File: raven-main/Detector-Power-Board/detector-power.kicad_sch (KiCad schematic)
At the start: 37 parts, among them J1 DeployLipo, J2 Conn_01x04, J9 UCLipo, U1 LT8330IS6-TRMPBF, U2 TPS22810DRV, U3 LM317LCLPRE3, U4 LM317LCLPRE3

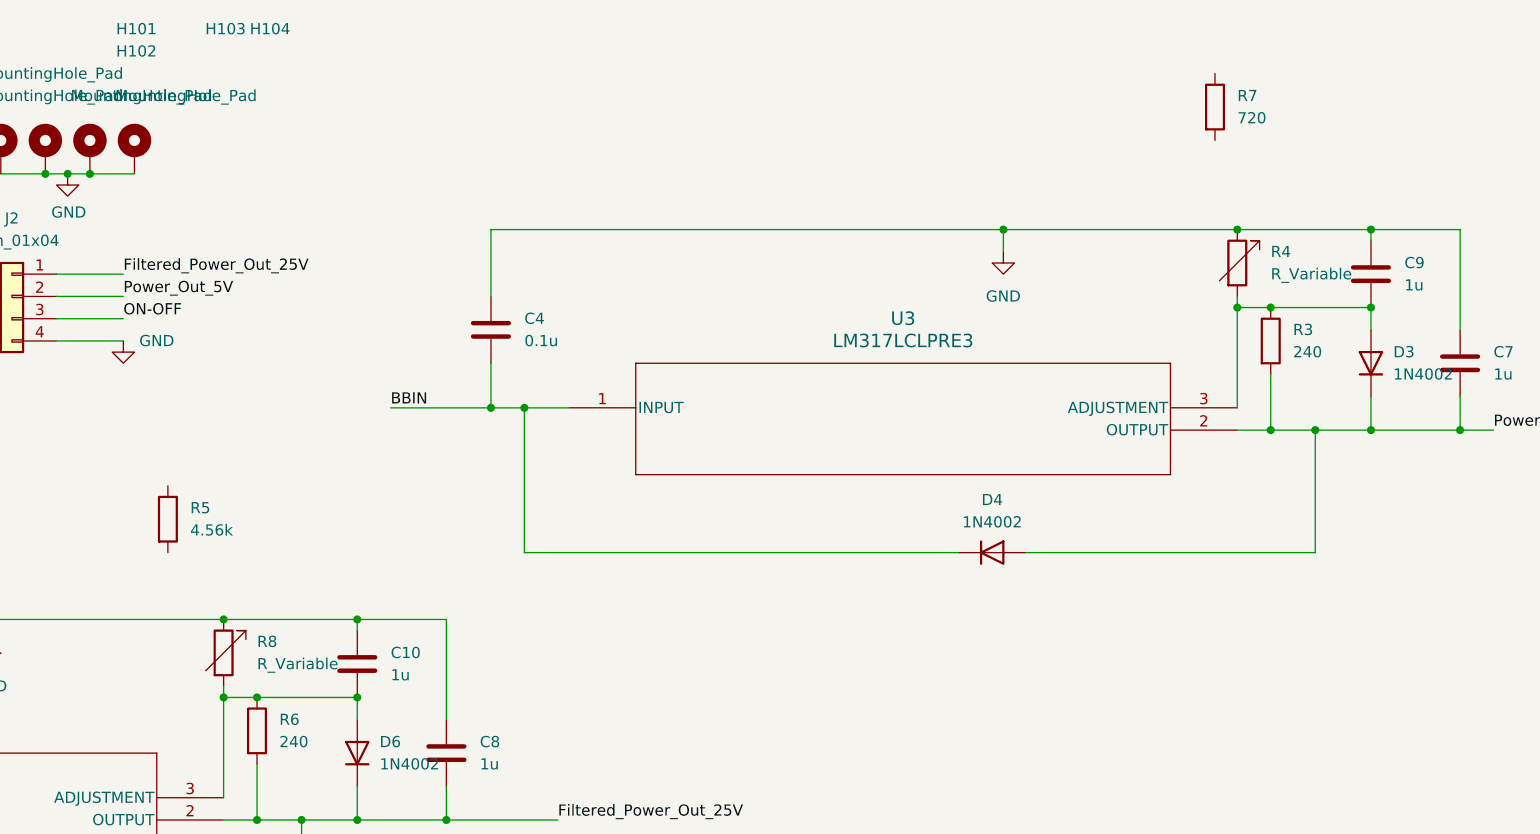
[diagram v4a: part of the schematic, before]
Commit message: More efficient routing
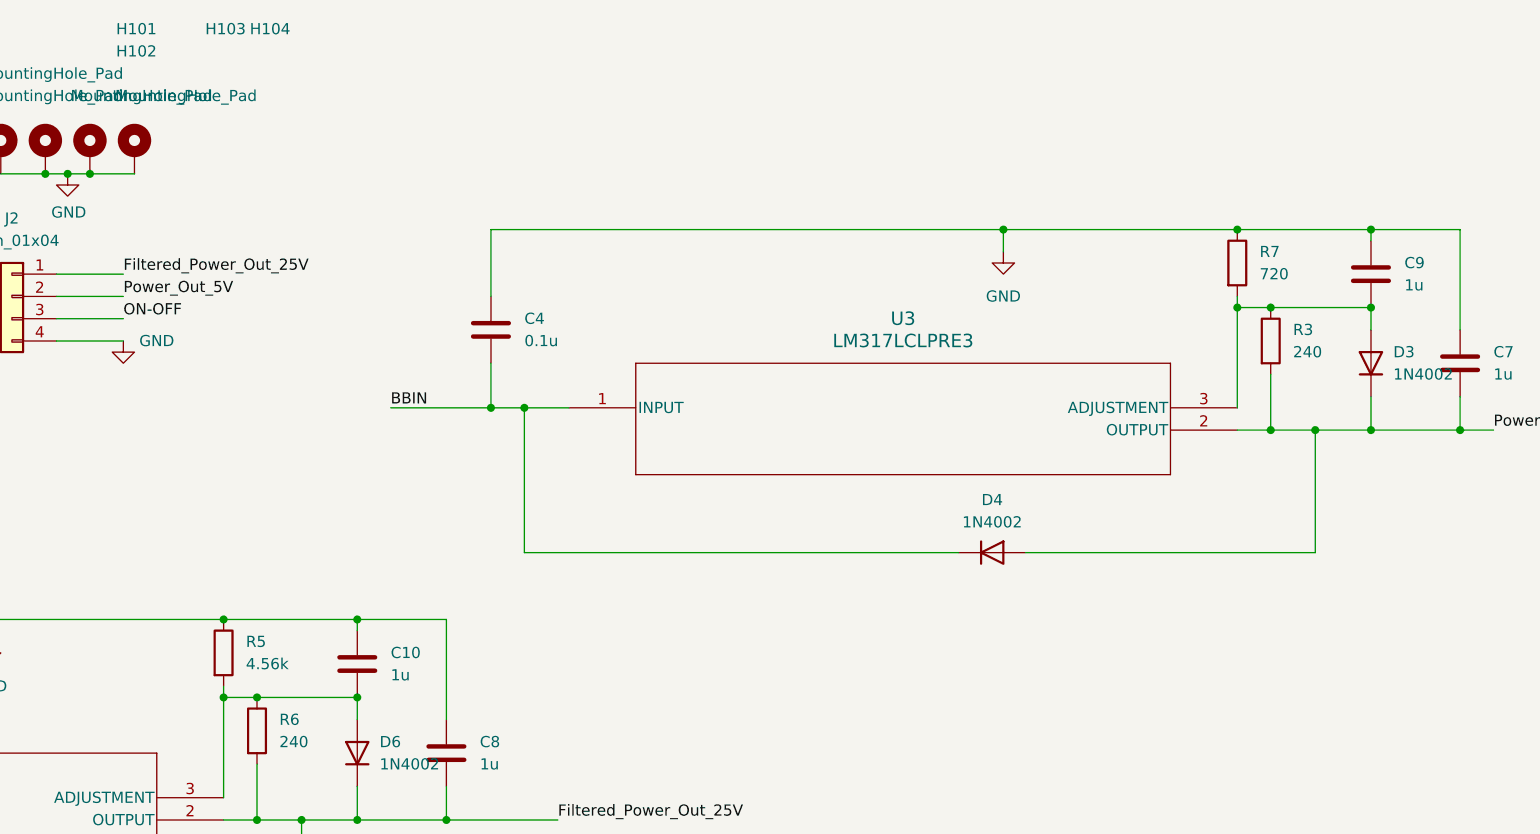
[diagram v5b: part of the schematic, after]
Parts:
- removed R4, R8: R_Variable, Resistor_SMD:R_0805_2012Metric, symbol Device:R_Variable
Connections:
- net GND: now also R5.1, R7.1
- net at C10.2, D6.2 (A), R6.1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: now also R5.2
- net at R7.2: now also C9.2, D3.2 (A), R3.1, U3.3 (ADJUSTMENT)
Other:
- moved on the sheet: R5, R7
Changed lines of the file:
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@@
 	(paper "A4")
 	(junction
+		(at 125.73 86.36)
+		(diameter 0)
+		(color 0 0 0 0)
+	)
+	(junction
 		(at 110.49 35.56)
 		(diameter 0)
@@
 	)
 	(junction
-		(at 125.73 86.36)
-		(diameter 0)
-		(color 0 0 0 0)
-	)
-	(junction
 		(at 151.13 109.22)
 		(diameter 0)
@@
 	(wire
 		(pts
-			(xy 125.73 86.36) (xy 140.97 86.36)
+			(xy 99.06 86.36) (xy 125.73 86.36)
 		)
 		(stroke
@@
 	(wire
 		(pts
+			(xy 125.73 86.36) (xy 140.97 86.36)
+		)
+		(stroke
+			(width 0)
+			(type default)
+		)
+	)
+	(wire
+		(pts
 			(xy 62.23 146.05) (xy 62.23 165.1)
 		)
@@
 	(wire
 		(pts
-			(xy 99.06 86.36) (xy 125.73 86.36)
-		)
-		(stroke
-			(width 0)
-			(type default)
-		)
-	)
-	(wire
-		(pts
 			(xy 48.26 40.64) (xy 53.34 40.64)
 		)
@@
 	)
 	(symbol
-		(lib_id "Device:R_Variable")
-		(at 125.73 90.17 0)
-		(unit 1)
-		(body_style 1)
-		(exclude_from_sim no)
-		(in_bom yes)
-		(on_board yes)
-		(in_pos_files yes)
-		(dnp no)
-		(fields_autoplaced yes)
-		(property "Reference" "R8"
-			(at 129.54 88.8999 0)
-			(show_name no)
-			(do_not_autoplace no)
-			(effects
-				(font
-					(size 1.27 1.27)
-				)
-				(justify left)
-			)
-		)
-		(property "Value" "R_Variable"
-			(at 129.54 91.4399 0)
-			(show_name no)
-			(do_not_autoplace no)
-			(effects
-				(font
-					(size 1.27 1.27)
-				)
-				(justify left)
-			)
-		)
-		(property "Footprint" "Resistor_SMD:R_0805_2012Metric"
-			(at 123.952 90.17 90)
-			(hide yes)
-			(show_name no)
-			(do_not_autoplace no)
-			(effects
-				(font
-					(size 1.27 1.27)
-				)
-			)
-		)
-		(property "Datasheet" ""
-			(at 125.73 90.17 0)
-			(hide yes)
-			(show_name no)
-			(do_not_autoplace no)
-			(effects
-				(font
-					(size 1.27 1.27)
-				)
-			)
-		)
-		(property "Description" "Variable resistor"
-			(at 125.73 90.17 0)
-			(hide yes)
-			(show_name no)
-			(do_not_autoplace no)
-			(effects
-				(font
-					(size 1.27 1.27)
-				)
-			)
-		)
-		(pin "1"
-		)
-		(pin "2"
-		)
-		(instances
-			(project "detector-power"
-				(path "/7c9dd221-ef7c-445c-ac49-d326ea2b82e0"
-					(reference "R8")
-					(unit 1)
-				)
-			)
-		)
-	)
-	(symbol
 		(lib_id "Connector:Conn_01x02_Male")
 		(at 31.75 40.64 0)
@@
 	(symbol
 		(lib_id "Device:R")
-		(at 238.76 27.94 0)
+		(at 241.3 45.72 0)
 		(unit 1)
 		(body_style 1)
@@
 		(fields_autoplaced yes)
 		(property "Reference" "R7"
-			(at 241.3 26.6699 0)
+			(at 243.84 44.4499 0)
 			(show_name no)
 			(do_not_autoplace no)
@@
 		)
 		(property "Value" "720"
-			(at 241.3 29.2099 0)
+			(at 243.84 46.9899 0)
 			(show_name no)
 			(do_not_autoplace no)
@@
 		)
 		(property "Footprint" "Resistor_SMD:R_0402_1005Metric"
-			(at 236.982 27.94 90)
+			(at 239.522 45.72 90)
 			(hide yes)
 			(show_name no)
@@
 		)
 		(property "Datasheet" ""
-			(at 238.76 27.94 0)
+			(at 241.3 45.72 0)
 			(hide yes)
 			(show_name no)
@@
 		)
 		(property "Description" "Resistor"
-			(at 238.76 27.94 0)
+			(at 241.3 45.72 0)
 			(hide yes)
 			(show_name no)
@@
 	(symbol
 		(lib_id "Device:R")
-		(at 119.38 74.93 0)
+		(at 125.73 90.17 0)
 		(unit 1)
 		(body_style 1)
@@
 		(fields_autoplaced yes)
 		(property "Reference" "R5"
-			(at 121.92 73.6599 0)
+			(at 128.27 88.8999 0)
 			(show_name no)
 			(do_not_autoplace no)
@@
 		)
 		(property "Value" "4.56k"
-			(at 121.92 76.1999 0)
+			(at 128.27 91.4399 0)
 			(show_name no)
 			(do_not_autoplace no)
@@
 		)
 		(property "Footprint" "Resistor_SMD:R_0402_1005Metric"
-			(at 117.602 74.93 90)
+			(at 123.952 90.17 90)
 			(hide yes)
 			(show_name no)
@@
 		)
 		(property "Datasheet" ""
-			(at 119.38 74.93 0)
+			(at 125.73 90.17 0)
 			(hide yes)
 			(show_name no)
@@
 		)
 		(property "Description" "Resistor"
-			(at 119.38 74.93 0)
+			(at 125.73 90.17 0)
 			(hide yes)
 			(show_name no)
@@
 					(unit 1)
 				)
-			)
-		)
-	)
-	(symbol
-		(lib_id "Device:R_Variable")
-		(at 241.3 45.72 0)
-		(unit 1)
-		(body_style 1)
-		(exclude_from_sim no)
-		(in_bom yes)
-		(on_board yes)
-		(in_pos_files yes)
-		(dnp no)
-		(fields_autoplaced yes)
-		(property "Reference" "R4"
-			(at 245.11 44.4499 0)
-			(show_name no)
-			(do_not_autoplace no)
-			(effects
-				(font
-					(size 1.27 1.27)
-				)
-				(justify left)
-			)
-		)
-		(property "Value" "R_Variable"
-			(at 245.11 46.9899 0)
-			(show_name no)
-			(do_not_autoplace no)
-			(effects
-				(font
-					(size 1.27 1.27)
-				)
-				(justify left)
-			)
-		)
-		(property "Footprint" "Resistor_SMD:R_0805_2012Metric"
-			(at 239.522 45.72 90)
-			(hide yes)
-			(show_name no)
-			(do_not_autoplace no)
-			(effects
-				(font
-					(size 1.27 1.27)
-				)
-			)
-		)
-		(property "Datasheet" ""
-			(at 241.3 45.72 0)
-			(hide yes)
-			(show_name no)
-			(do_not_autoplace no)
-			(effects
-				(font
-					(size 1.27 1.27)
-				)
-			)
-		)
-		(property "Description" "Variable resistor"
-			(at 241.3 45.72 0)
-			(hide yes)
-			(show_name no)
-			(do_not_autoplace no)
-			(effects
-				(font
-					(size 1.27 1.27)
-				)
-			)
-		)
-		(pin "1"
-		)
-		(pin "2"
-		)
-		(instances
-			(project "detector-power"
-				(path "/7c9dd221-ef7c-445c-ac49-d326ea2b82e0"
-					(reference "R4")
-					(unit 1)
-				)
